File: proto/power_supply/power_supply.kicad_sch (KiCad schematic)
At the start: 2 parts, among them J1 Conn_01x02, J2 Conn_01x02

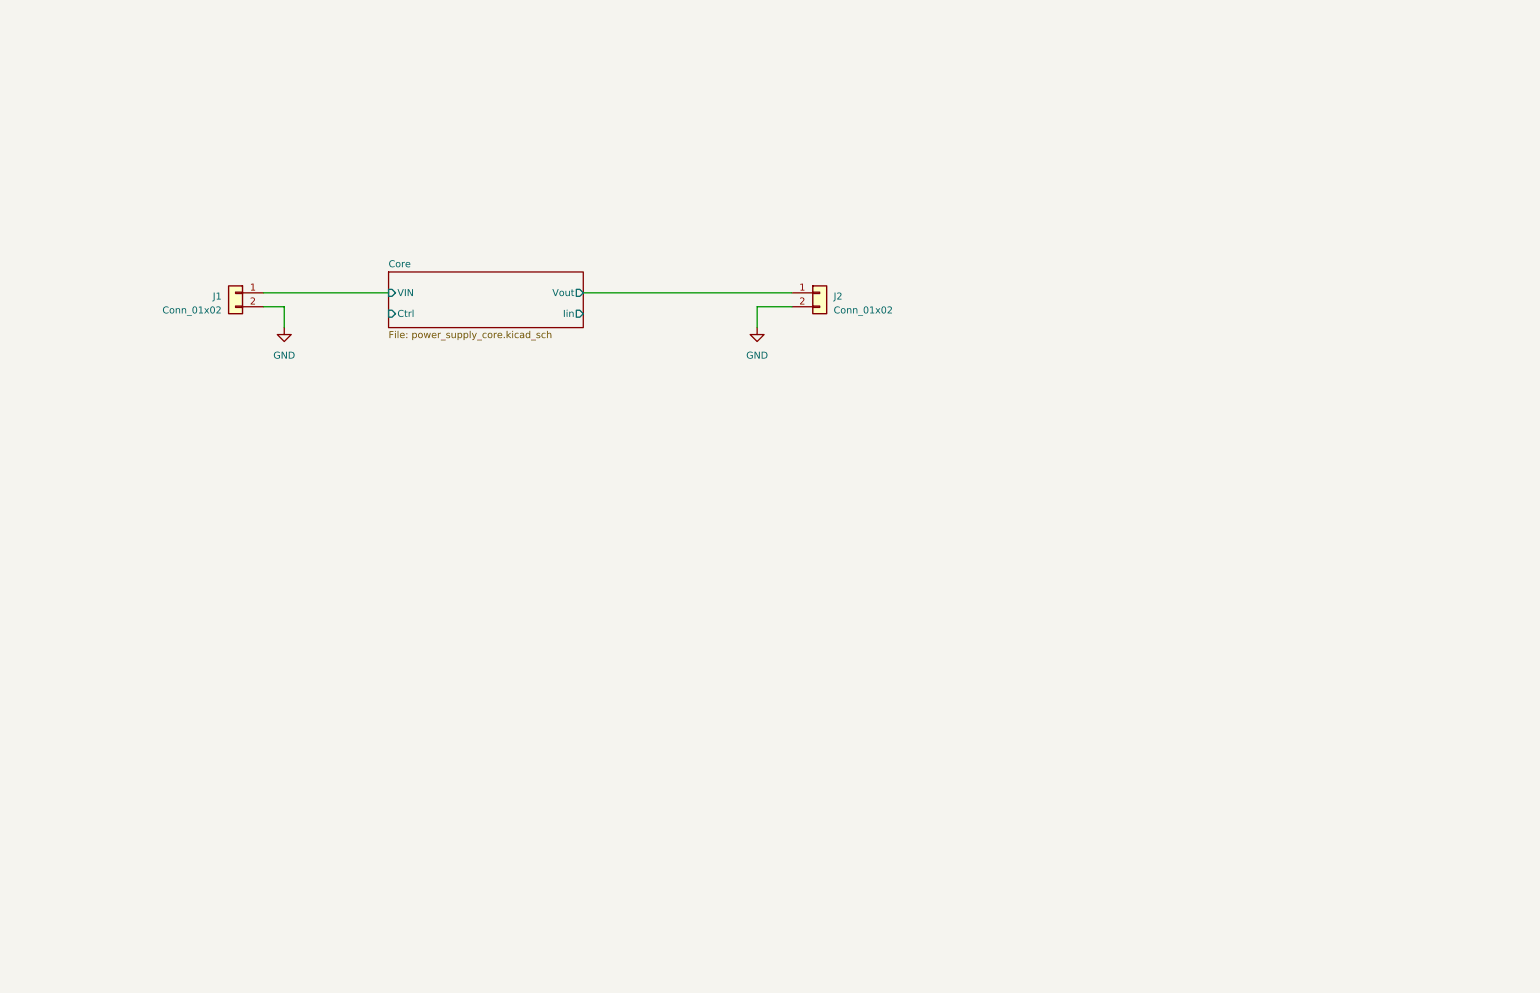
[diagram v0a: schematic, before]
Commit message: Global alimentation update
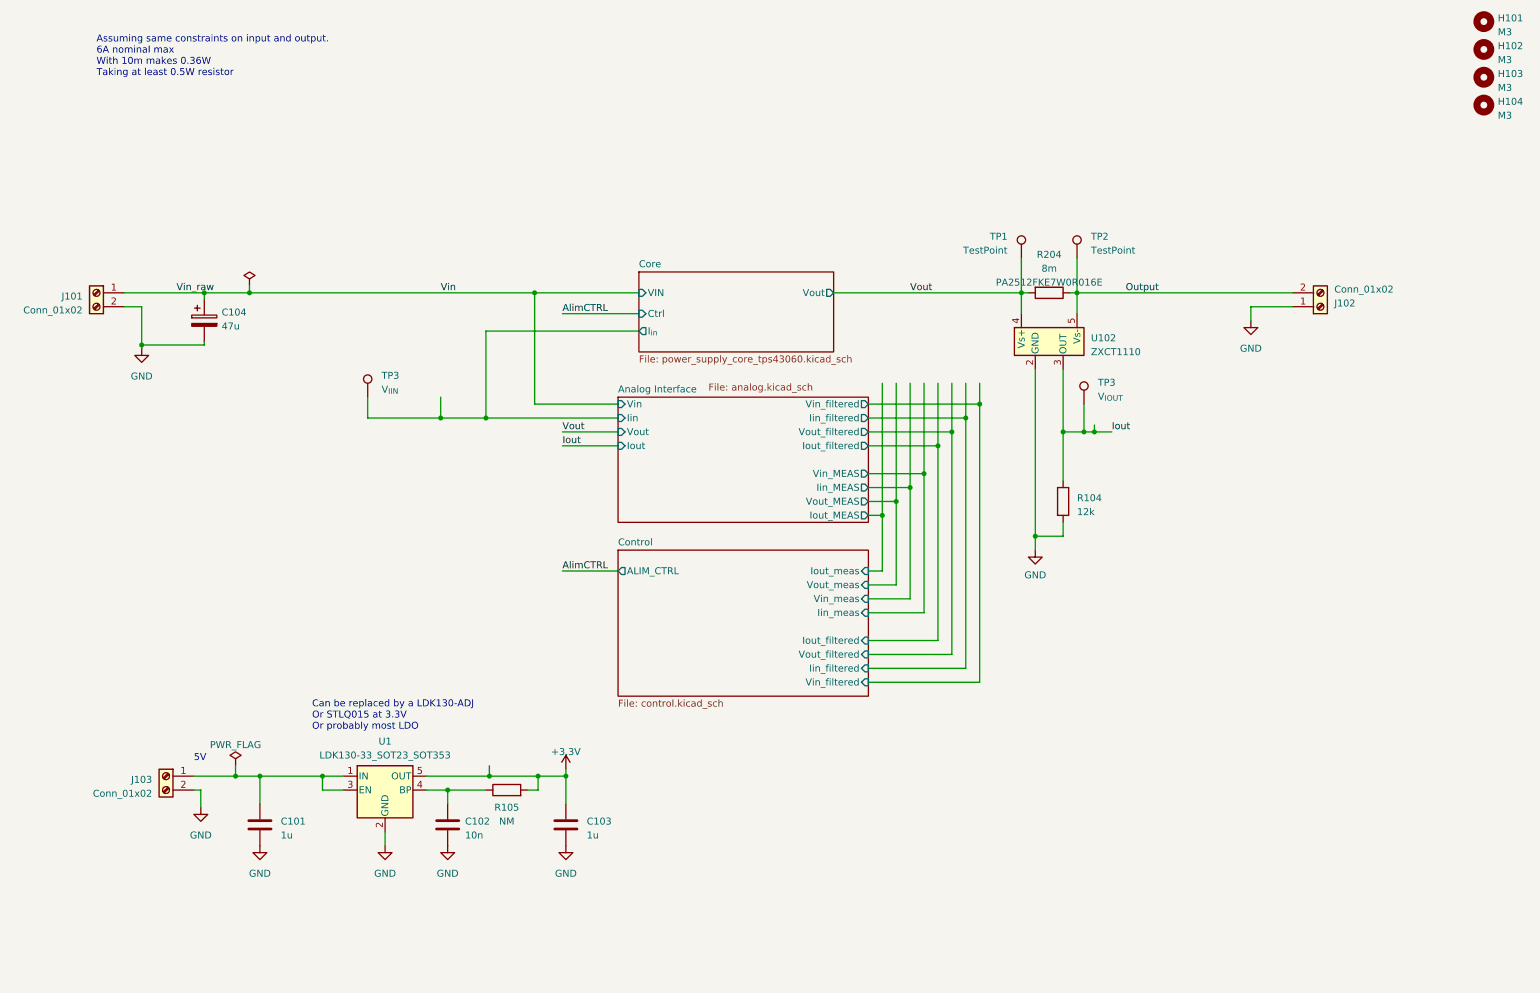
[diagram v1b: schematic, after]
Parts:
- added C101, C103: 1u, Capacitor_SMD:C_0805_2012Metric, symbol Device:C
- added C102: 10n, Capacitor_SMD:C_0805_2012Metric, symbol Device:C
- added C104: 47u, Capacitor_THT:CP_Radial_D5.0mm_P2.50mm, symbol Device:C_Polarized
- added H101, H102, H103, H104: M3, MountingHole:MountingHole_3.2mm_M3, symbol Mechanical:MountingHole
- added J103: Conn_01x02, TerminalBlock_WAGO:TerminalBlock_WAGO_236-402_1x02_P5.00mm_45Degree, symbol Connector:Screw_Terminal_01x02
- added R104: 12k, Resistor_SMD:R_0805_2012Metric, symbol Device:R
- added R105: NM, Resistor_SMD:R_0805_2012Metric, symbol Device:R
- added R204: 8m, Resistor_SMD:R_2512_6332Metric, symbol Device:R
- added TP1, TP2: TestPoint, TestPoint:TestPoint_Keystone_5010-5014_Multipurpose, symbol Connector:TestPoint
- added TP3: V_{IIN}, TestPoint:TestPoint_Keystone_5010-5014_Multipurpose, symbol Connector:TestPoint
- added TP3: V_{IOUT}, TestPoint:TestPoint_Keystone_5010-5014_Multipurpose, symbol Connector:TestPoint
- added U1: LDK130-33_SOT23_SOT353, Package_TO_SOT_SMD:SOT-23-5, symbol Regulator_Linear:LDK130-33_SOT23_SOT353
- added U102: ZXCT1110, Package_TO_SOT_SMD:SOT-23-5, symbol Amplifier_Current:ZXCT1110
- J101: renamed from J1; footprint (none) -> TerminalBlock_WAGO:TerminalBlock_WAGO_236-402_1x02_P5.00mm_45Degree; symbol Connector_Generic:Conn_01x02 -> Connector:Screw_Terminal_01x02
- J102: renamed from J2; footprint (none) -> TerminalBlock_WAGO:TerminalBlock_WAGO_236-402_1x02_P5.00mm_45Degree; symbol Connector_Generic:Conn_01x02 -> Connector:Screw_Terminal_01x02
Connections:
- net Core/Vout is gone; now on net GND: J102.1 (Pin_1)
- net GND: now also C101.2, C102.2, C103.2, C104.2, J103.2 (Pin_2), R104.2, U1.2 (GND), U102.2 (GND); no longer J102.2 (Pin_2)
- net Core/VIN renamed Vin
- net Vin: now also C104.1
- new net: C101.1, J103.1 (Pin_1), U1.1 (IN), U1.3 (EN)
- new net: C102.1, R105.1, U1.4 (BP)
- new net +3.3V: C103.1, R105.2, U1.5 (OUT)
- new net Analog Interface/Iin: TP3.1
- new net Iout: R104.1, TP3.1, U102.3 (OUT)
- new net Output: J102.2 (Pin_2), R204.1, TP2.1, U102.5 (Vs-)
- new net Vout: R204.2, TP1.1, U102.4 (Vs+)
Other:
- added sheet Analog Interface (analog.kicad_sch)
- added sheet Control (control.kicad_sch)
- sheet Core: file power_supply_core.kicad_sch -> power_supply_core_tps43060.kicad_sch
- sheet Core ports: added I_{in}; removed Iin
- note added: "5V"
- note added: "Assuming same constraints on input and output. 6A nominal max With 10m makes 0.36W Taking at least 0.5W resistor"
- note added: "Can be replaced by a LDK130-ADJ Or STLQ015 at 3.3V Or probably most LDO"

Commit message: Finish alim sch, start PCB
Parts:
- renumbered C104 to C101, C101 to C102, C102 to C103, C103 to C104, R104 to R102, R105 to R103, U102 to U101

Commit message: Improve overall
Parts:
- added TP1 (x2), TP2: TestPoint, TestPoint:TestPoint_Keystone_5010-5014_Multipurpose, symbol Connector:TestPoint
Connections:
- net +3.3V: now also TP1.1
- net GND: now also TP2.1
- net at C102.1, J103.1 (Pin_1), U1.1 (IN)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: now also TP1.1
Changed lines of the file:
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@@
   (junction (at 175.26 91.44) (diameter 0) (color 0 0 0 0)
   )
+  (junction (at 101.6 154.305) (diameter 0) (color 0 0 0 0)
+  )
   (junction (at 187.96 66.04) (diameter 0) (color 0 0 0 0)
   )
@@
   (junction (at 165.1 104.14) (diameter 0) (color 0 0 0 0)
   )
+  (junction (at 52.07 154.305) (diameter 0) (color 0 0 0 0)
+  )
   (junction (at 172.72 93.98) (diameter 0) (color 0 0 0 0)
   )
@@
     (stroke (width 0) (type default))
   )
+  (wire (pts (xy 52.07 147.32) (xy 52.07 154.305))
+    (stroke (width 0) (type default))
+  )
   (wire (pts (xy 36.83 154.305) (xy 44.45 154.305))
     (stroke (width 0) (type default))
@@
     (stroke (width 0) (type default))
   )
-  (wire (pts (xy 48.895 154.305) (xy 60.325 154.305))
+  (wire (pts (xy 48.895 154.305) (xy 52.07 154.305))
     (stroke (width 0) (type default))
   )
@@
     (stroke (width 0) (type default))
   )
+  (wire (pts (xy 101.6 147.32) (xy 101.6 154.305))
+    (stroke (width 0) (type default))
+  )
   (wire (pts (xy 195.58 91.44) (xy 195.58 100.33))
     (stroke (width 0) (type default))
@@
     (stroke (width 0) (type default))
   )
-  (wire (pts (xy 99.695 154.305) (xy 104.775 154.305))
+  (wire (pts (xy 99.695 154.305) (xy 101.6 154.305))
     (stroke (width 0) (type default))
   )
@@
     (stroke (width 0) (type default))
   )
+  (wire (pts (xy 52.07 154.305) (xy 60.325 154.305))
+    (stroke (width 0) (type default))
+  )
   (wire (pts (xy 160.02 93.98) (xy 172.72 93.98))
     (stroke (width 0) (type default))
@@
   )
   (wire (pts (xy 160.02 121.92) (xy 167.64 121.92))
+    (stroke (width 0) (type default))
+  )
+  (wire (pts (xy 101.6 154.305) (xy 104.775 154.305))
     (stroke (width 0) (type default))
   )
@@
     )
   )
+  (symbol (lib_id "Connector:TestPoint") (at 233.68 104.775 0) (unit 1)
+    (in_bom yes) (on_board yes) (dnp no) (fields_autoplaced)
+    (property "Reference" "TP2" (at 236.22 100.838 0)
+      (effects (font (size 1.27 1.27)) (justify left))
+    )
+    (property "Value" "TestPoint" (at 236.22 103.378 0)
+      (effects (font (size 1.27 1.27)) (justify left))
+    )
+    (property "Footprint" "TestPoint:TestPoint_Keystone_5010-5014_Multipurpose" (at 238.76 104.775 0)
+      (effects (font (size 1.27 1.27)) hide)
+    )
+    (property "Datasheet" "~" (at 238.76 104.775 0)
+      (effects (font (size 1.27 1.27)) hide)
+    )
+    (pin "1")
+    (instances
+      (project "power_supply"
+        (path "/e87df9ac-84db-475c-955a-f1fa477bbb69/91eacb21-145b-4d7f-8dcd-2105a1b91924"
+          (reference "TP2") (unit 1)
+        )
+        (path "/e87df9ac-84db-475c-955a-f1fa477bbb69"
+          (reference "TP107") (unit 1)
+        )
+      )
+    )
+  )
   (symbol (lib_id "Device:R") (at 195.58 104.14 0) (unit 1)
     (in_bom yes) (on_board yes) (dnp no) (fields_autoplaced)
@@
     )
   )
+  (symbol (lib_id "Connector:TestPoint") (at 101.6 147.32 0) (unit 1)
+    (in_bom yes) (on_board yes) (dnp no) (fields_autoplaced)
+    (property "Reference" "TP1" (at 99.06 143.383 0)
+      (effects (font (size 1.27 1.27)) (justify right))
+    )
+    (property "Value" "TestPoint" (at 99.06 145.923 0)
+      (effects (font (size 1.27 1.27)) (justify right))
+    )
+    (property "Footprint" "TestPoint:TestPoint_Keystone_5010-5014_Multipurpose" (at 106.68 147.32 0)
+      (effects (font (size 1.27 1.27)) hide)
+    )
+    (property "Datasheet" "~" (at 106.68 147.32 0)
+      (effects (font (size 1.27 1.27)) hide)
+    )
+    (pin "1")
+    (instances
+      (project "power_supply"
+        (path "/e87df9ac-84db-475c-955a-f1fa477bbb69/91eacb21-145b-4d7f-8dcd-2105a1b91924"
+          (reference "TP1") (unit 1)
+        )
+        (path "/e87df9ac-84db-475c-955a-f1fa477bbb69"
+          (reference "TP106") (unit 1)
+        )
+      )
+    )
+  )
   (symbol (lib_id "power:GND") (at 27.305 76.2 0) (unit 1)
     (in_bom yes) (on_board yes) (dnp no) (fields_autoplaced)
@@
         (path "/e87df9ac-84db-475c-955a-f1fa477bbb69"
           (reference "C101") (unit 1)
+        )
+      )
+    )
+  )
+  (symbol (lib_id "Connector:TestPoint") (at 52.07 147.32 0) (unit 1)
+    (in_bom yes) (on_board yes) (dnp no) (fields_autoplaced)
+    (property "Reference" "TP1" (at 49.53 143.383 0)
+      (effects (font (size 1.27 1.27)) (justify right))
+    )
+    (property "Value" "TestPoint" (at 49.53 145.923 0)
+      (effects (font (size 1.27 1.27)) (justify right))
+    )
+    (property "Footprint" "TestPoint:TestPoint_Keystone_5010-5014_Multipurpose" (at 57.15 147.32 0)
+      (effects (font (size 1.27 1.27)) hide)
+    )
+    (property "Datasheet" "~" (at 57.15 147.32 0)
+      (effects (font (size 1.27 1.27)) hide)
+    )
+    (pin "1")
+    (instances
+      (project "power_supply"
+        (path "/e87df9ac-84db-475c-955a-f1fa477bbb69/91eacb21-145b-4d7f-8dcd-2105a1b91924"
+          (reference "TP1") (unit 1)
+        )
+        (path "/e87df9ac-84db-475c-955a-f1fa477bbb69"
+          (reference "TP105") (unit 1)
         )
       )
@@
         )
       )
+    )
+  )
+  (symbol (lib_name "GND_2") (lib_id "power:GND") (at 233.68 104.775 0) (unit 1)
+    (in_bom yes) (on_board yes) (dnp no) (fields_autoplaced)
+    (property "Reference" "#PWR0110" (at 233.68 111.125 0)
+      (effects (font (size 1.27 1.27)) hide)
+    )
+    (property "Value" "GND" (at 233.68 109.22 0)
+      (effects (font (size 1.27 1.27)))
+    )
+    (property "Footprint" "" (at 233.68 104.775 0)
+      (effects (font (size 1.27 1.27)) hide)
+    )
+    (property "Datasheet" "" (at 233.68 104.775 0)
+      (effects (font (size 1.27 1.27)) hide)
+    )
+    (pin "1")
+    (instances
+      (project "power_supply"
+        (path "/e87df9ac-84db-475c-955a-f1fa477bbb69"
+          (reference "#PWR0110") (unit 1)
+        )
+      )

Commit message: Update with additional PSU from output
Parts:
- added C105: 100n, Capacitor_SMD:C_0805_2012Metric, symbol Device:C
- added C106, C107: 10u, Capacitor_SMD:C_0805_2012Metric, symbol Device:C
- added JP101: SolderJumper_3_Open, Jumper:SolderJumper-3_P2.0mm_Open_TrianglePad1.0x1.5mm, symbol Jumper:SolderJumper_3_Open
- added JP102: EN DIG SUPPLY, Jumper:SolderJumper-2_P1.3mm_Open_TrianglePad1.0x1.5mm, symbol Jumper:SolderJumper_2_Open
- added JP103: LINK_GND, Jumper:SolderJumper-2_P1.3mm_Open_TrianglePad1.0x1.5mm, symbol Jumper:SolderJumper_2_Open
- added L101: 3.3u, Inductor_SMD:L_6.3x6.3_H3, symbol Device:L
- added R104: 22k, Resistor_SMD:R_0805_2012Metric, symbol Device:R
- added R105: 3.3k, Resistor_SMD:R_0805_2012Metric, symbol Device:R
- added R106: 10k, Resistor_SMD:R_0805_2012Metric, symbol Device:R
- added U103: LMR51430, Package_TO_SOT_SMD:SOT-23-6, symbol power_supply:LMR51430
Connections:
- net GND: now also C106.2, C107.2, JP103.1 (A), JP103.2 (B), R105.1, R106.1, U103.1 (GND)
- net Output: now also JP102.2 (B), U103.3 (VIN)
- net at C102.1, TP1.1, U1.1 (IN)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: now also JP101.2 (C); no longer J103.1 (Pin_1)
- new net: J103.1 (Pin_1), JP101.1 (A)
- new net: JP102.1 (A), R106.2, U103.5 (EN)
- new net: C106.1, C107.1, JP101.3 (B), L101.2, R104.2
- new net: C105.2, L101.1, U103.2 (SW)
- new net: R104.1, R105.2, U103.4 (FB)
- new net: C105.1, U103.6 (BOOT)
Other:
- moved on the sheet: C102, C103, C104, J103, R103, TP1, U1

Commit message: Final edit before v1 release
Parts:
- added TP2: TestPoint, TestPoint:TestPoint_Keystone_5010-5014_Multipurpose, symbol Connector:TestPoint
- L101: footprint Inductor_SMD:L_6.3x6.3_H3 -> power_supply:VLS3015CX; MPN (none) -> VLS3015CX-3R3M-1
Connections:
- net GND: now also TP2.1
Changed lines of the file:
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@@
+    )
+  )
+  (symbol (lib_name "GND_2") (lib_id "power:GND") (at 248.285 104.775 0) (unit 1)
+    (in_bom yes) (on_board yes) (dnp no) (fields_autoplaced)
+    (property "Reference" "#PWR0117" (at 248.285 111.125 0)
+      (effects (font (size 1.27 1.27)) hide)
+    )
+    (property "Value" "GND" (at 248.285 109.22 0)
+      (effects (font (size 1.27 1.27)))
+    )
+    (property "Footprint" "" (at 248.285 104.775 0)
+      (effects (font (size 1.27 1.27)) hide)
+    )
+    (property "Datasheet" "" (at 248.285 104.775 0)
+      (effects (font (size 1.27 1.27)) hide)
+    )
+    (pin "1")
+    (instances
+      (project "power_supply"
+        (path "/e87df9ac-84db-475c-955a-f1fa477bbb69"
+          (reference "#PWR0117") (unit 1)
+        )
+      )
     )
   )
@@
   )
   (symbol (lib_id "Device:L") (at 74.295 144.145 90) (unit 1)
-    (in_bom yes) (on_board yes) (dnp no) (fields_autoplaced)
+    (in_bom yes) (on_board yes) (dnp no)
     (property "Reference" "L101" (at 74.295 139.7 90)
       (effects (font (size 1.27 1.27)))
@@
       (effects (font (size 1.27 1.27)))
     )
-    (property "Footprint" "Inductor_SMD:L_6.3x6.3_H3" (at 74.295 144.145 0)
-      (effects (font (size 1.27 1.27)) hide)
-    )
-    (property "Datasheet" "~" (at 74.295 144.145 0)
-      (effects (font (size 1.27 1.27)) hide)
-    )
-    (property "MPN" "" (at 74.295 144.145 0)
+    (property "Footprint" "power_supply:VLS3015CX" (at 74.295 144.145 0)
+      (effects (font (size 1.27 1.27)) hide)
+    )
+    (property "Datasheet" "https://product.tdk.com/system/files/dam/doc/product/inductor/inductor/smd/catalog/inductor_commercial_power_vls3015cx-1_en.pdf" (at 74.295 144.145 0)
+      (effects (font (size 1.27 1.27)) hide)
+    )
+    (property "MPN" "VLS3015CX-3R3M-1" (at 74.295 137.16 90)
       (effects (font (size 1.27 1.27)))
     )
@@
         )
       )
+    )
+  )
+  (symbol (lib_id "Connector:TestPoint") (at 248.285 104.775 0) (unit 1)
+    (in_bom yes) (on_board yes) (dnp no) (fields_autoplaced)
+    (property "Reference" "TP2" (at 250.825 100.838 0)
+      (effects (font (size 1.27 1.27)) (justify left))
+    )
+    (property "Value" "TestPoint" (at 250.825 103.378 0)
+      (effects (font (size 1.27 1.27)) (justify left))
+    )
+    (property "Footprint" "TestPoint:TestPoint_Keystone_5010-5014_Multipurpose" (at 253.365 104.775 0)
+      (effects (font (size 1.27 1.27)) hide)
+    )
+    (property "Datasheet" "~" (at 253.365 104.775 0)
+      (effects (font (size 1.27 1.27)) hide)
+    )
+    (pin "1")
+    (instances
+      (project "power_supply"
+        (path "/e87df9ac-84db-475c-955a-f1fa477bbb69/91eacb21-145b-4d7f-8dcd-2105a1b91924"
+          (reference "TP2") (unit 1)
+        )
+        (path "/e87df9ac-84db-475c-955a-f1fa477bbb69"
+          (reference "TP108") (unit 1)
+        )
+      )
